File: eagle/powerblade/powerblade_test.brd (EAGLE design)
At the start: 27.9 x 27.9 mm, 78 parts, among them J1 JTAG_14PIN_IDC-NL, J21 AC_INFILM, Q1 2N7002, U1 TPS62122, U2 AD524, U3 MSP430FR5738, U4 LTC5800, U5 MAX9910, U6 MAX9910

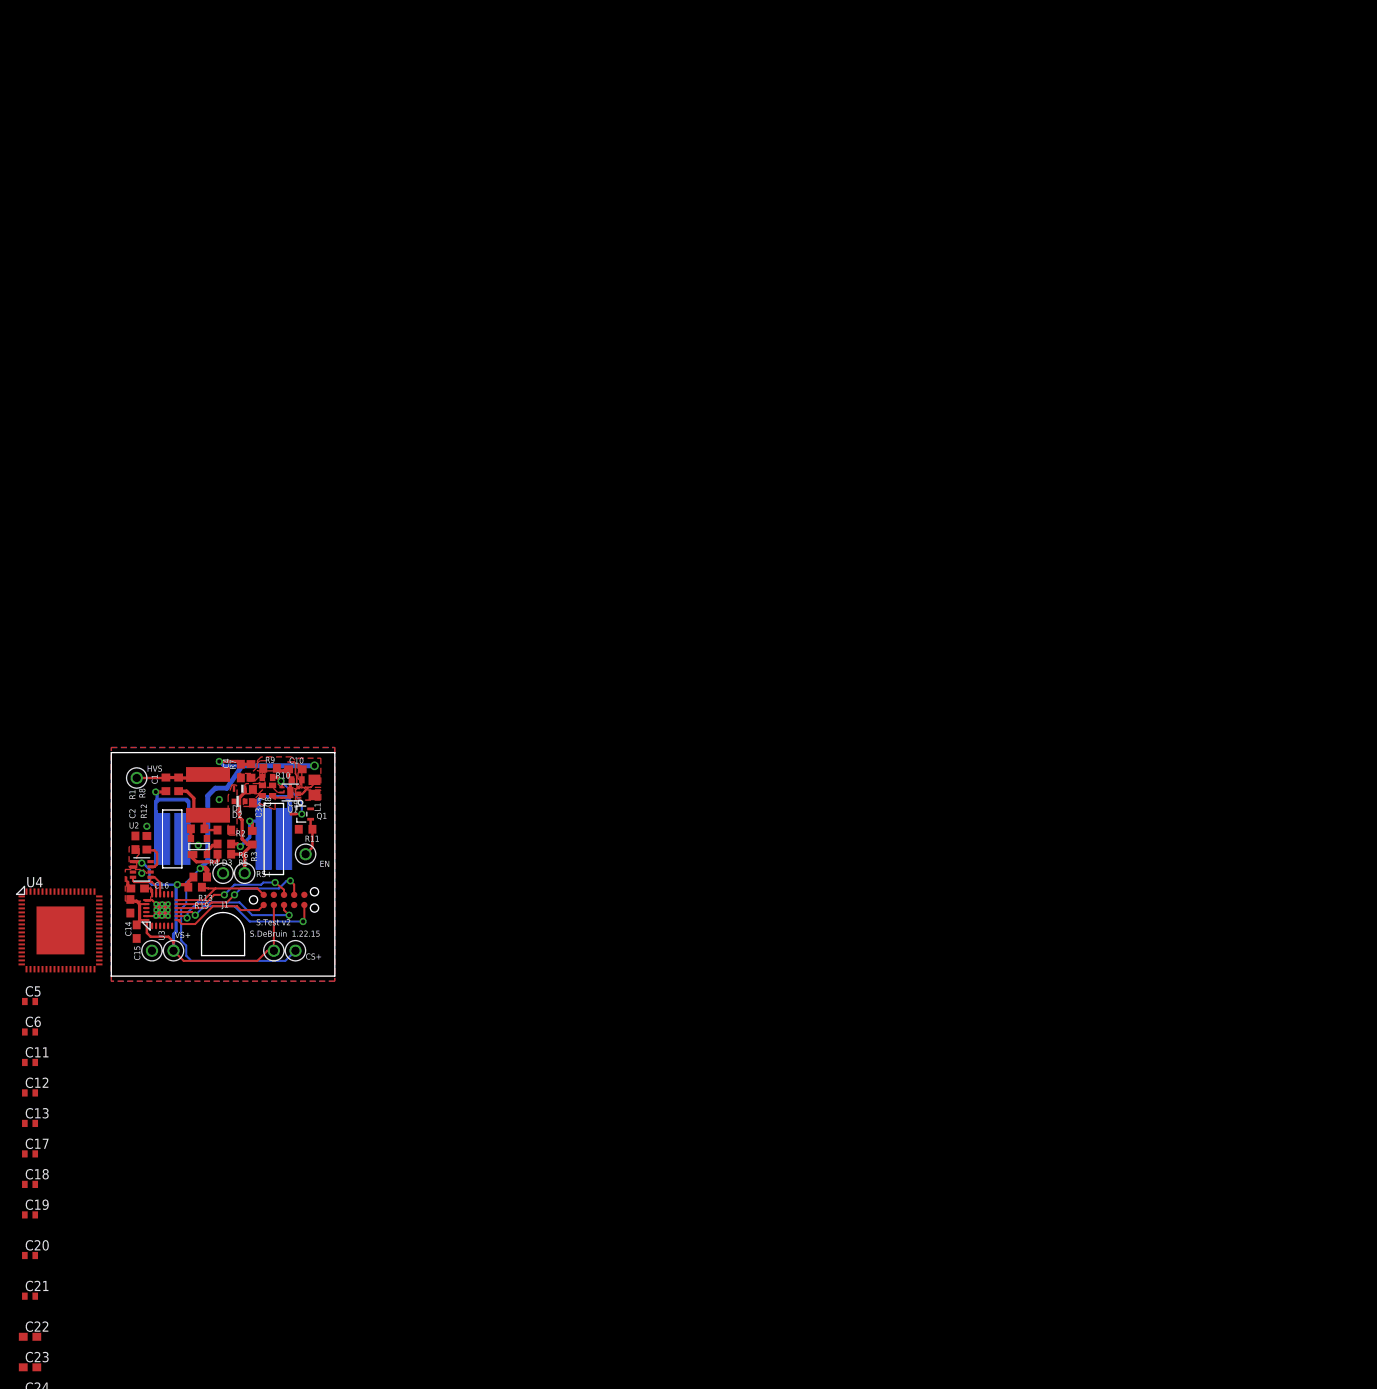
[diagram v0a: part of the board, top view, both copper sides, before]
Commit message: added outline for powerblade test board
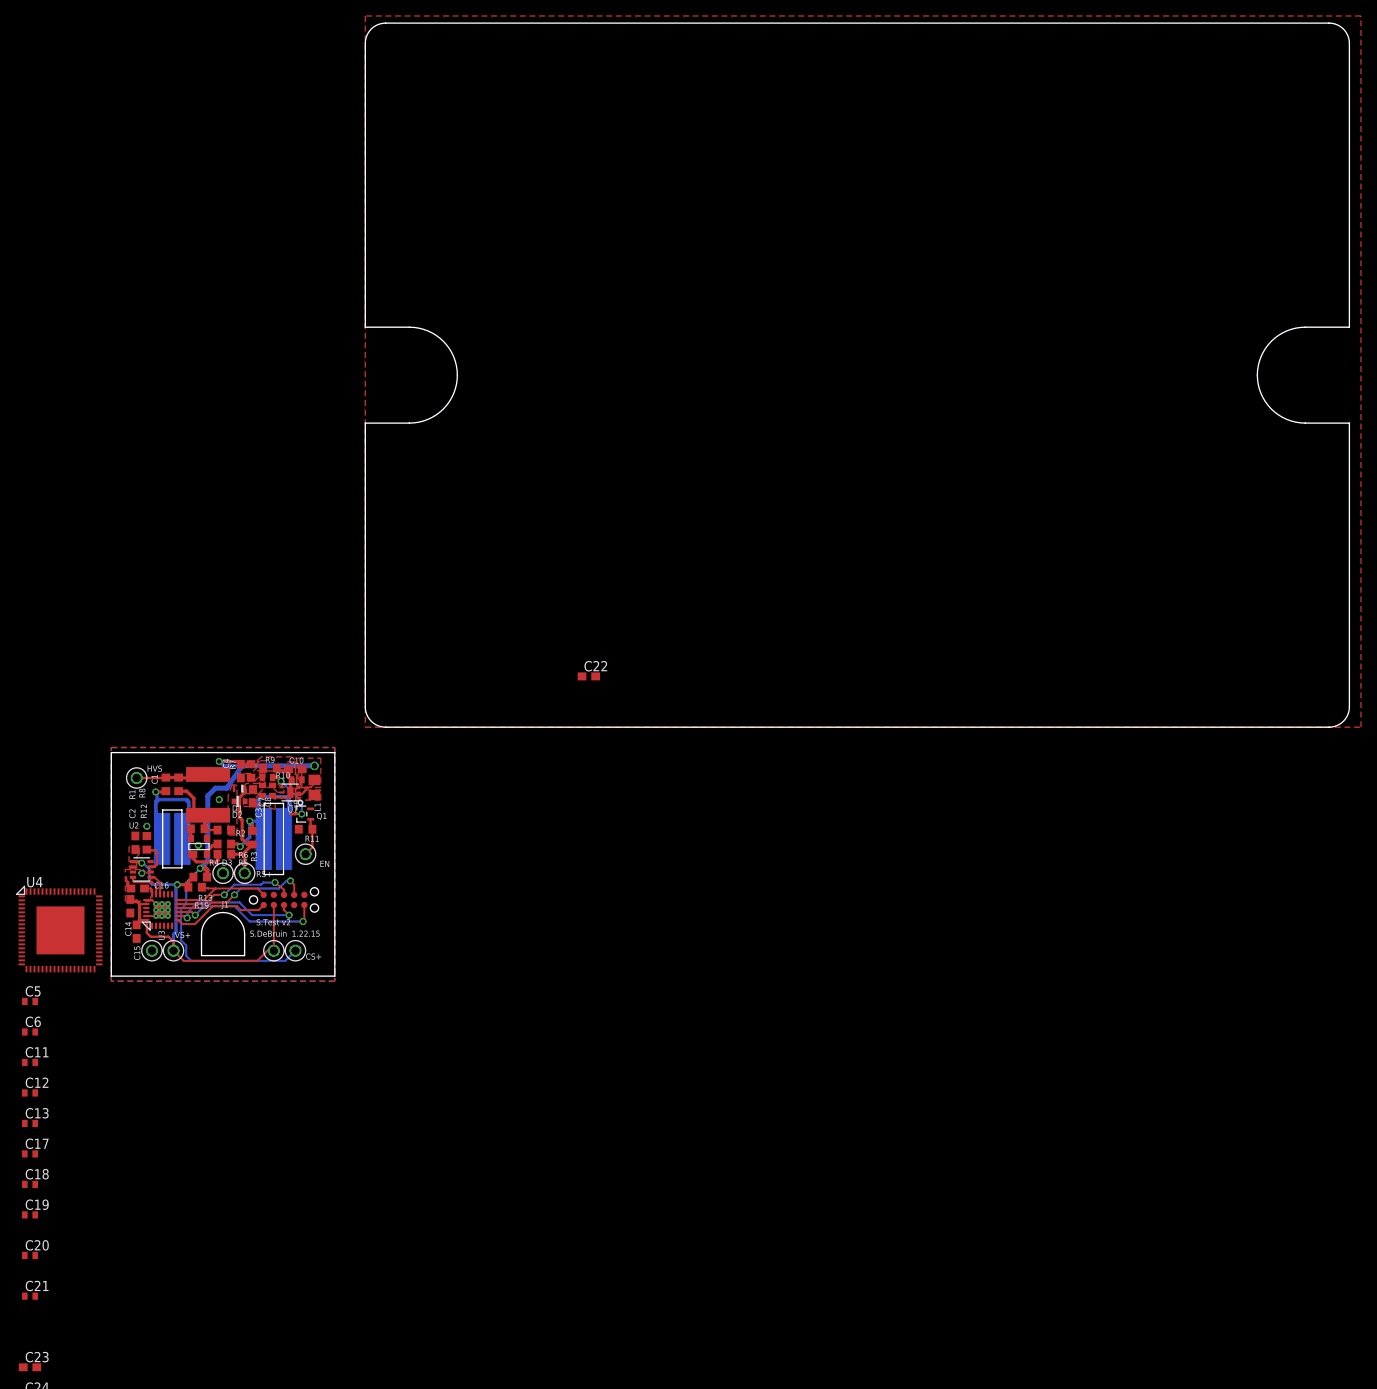
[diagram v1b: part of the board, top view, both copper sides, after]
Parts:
- moved C22 108.1 mm to (27.9, 6.35)
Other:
- board size 27.9 x 27.9 mm -> 123 x 88 mm
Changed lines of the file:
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@@
 <?xml version="1.0" encoding="utf-8"?>
 <!DOCTYPE eagle SYSTEM "eagle.dtd">
-<eagle version="6.5.0">
+<eagle version="6.3">
 <drawing>
 <settings>
@@
 <setting verticaltext="up"/>
 </settings>
-<grid distance="0.05" unitdist="inch" unit="mm" style="lines" multiple="1" display="no" altdistance="6.25" altunitdist="mil" altunit="mil"/>
+<grid distance="0.05" unitdist="inch" unit="mil" style="lines" multiple="1" display="no" altdistance="6.25" altunitdist="mil" altunit="mil"/>
 <layers>
 <layer number="1" name="Top" color="4" fill="1" visible="yes" active="yes"/>
@@
 <text x="-9.2075" y="-26.19375" size="0.762" layer="21">1.22.15</text>
 <text x="-13.6525" y="-24.765" size="0.762" layer="21">S.Test v2</text>
+<wire x1="2.54" y1="0" x2="0" y2="2.54" width="0" layer="20" curve="-90"/>
+<wire x1="0" y1="85.471" x2="2.54" y2="88.011" width="0" layer="20" curve="-90"/>
+<wire x1="2.54" y1="88.011" x2="120.4722" y2="88.011" width="0" layer="20"/>
+<wire x1="120.4722" y1="88.011" x2="123.0122" y2="85.471" width="0" layer="20" curve="-90"/>
+<wire x1="123.0122" y1="2.54" x2="120.4722" y2="0" width="0" layer="20" curve="-90"/>
+<wire x1="120.4722" y1="0" x2="2.54" y2="0" width="0" layer="20"/>
+<wire x1="0" y1="2.54" x2="0" y2="38.0111" width="0" layer="20"/>
+<wire x1="0" y1="38.0111" x2="5.5118" y2="38.0111" width="0" layer="20"/>
+<wire x1="5.5118" y1="38.0111" x2="11.5062" y2="44.0055" width="0" layer="20" curve="90"/>
+<wire x1="11.5062" y1="44.0055" x2="5.5118" y2="49.9999" width="0" layer="20" curve="90"/>
+<wire x1="5.5118" y1="49.9999" x2="0" y2="49.9999" width="0" layer="20"/>
+<wire x1="0" y1="49.9999" x2="0" y2="85.471" width="0" layer="20"/>
+<wire x1="123.0122" y1="2.54" x2="123.0122" y2="38.0111" width="0" layer="20"/>
+<wire x1="123.0122" y1="38.0111" x2="117.5004" y2="38.0111" width="0" layer="20"/>
+<wire x1="117.5004" y1="38.0111" x2="111.506" y2="44.0055" width="0" layer="20" curve="-90"/>
+<wire x1="111.506" y1="44.0055" x2="117.5004" y2="49.9999" width="0" layer="20" curve="-90"/>
+<wire x1="117.5004" y1="49.9999" x2="123.0122" y2="49.9999" width="0" layer="20"/>
+<wire x1="123.0122" y1="49.9999" x2="123.0122" y2="85.471" width="0" layer="20"/>
 </plain>
 <attributes>
@@
 <element name="C20" library="rcl" package="C0402" value="56nF" x="-41.91" y="-66.04"/>
 <element name="C21" library="rcl" package="C0402" value="56nF" x="-41.91" y="-71.12"/>
-<element name="C22" library="rcl" package="C0603" value="0.1uF" x="-41.91" y="-76.2"/>
+<element name="C22" library="rcl" package="C0603" value="0.1uF" x="27.94" y="6.35"/>
 <element name="C23" library="rcl" package="C0603" value="0.47uF" x="-41.91" y="-80.01"/>
 <element name="C24" library="rcl" package="C0603" value="0.22uF" x="-41.91" y="-83.82"/>
@@
 <contactref element="U5" pad="P2"/>
 <contactref element="SV1" pad="8"/>
+<polygon width="0.2032" layer="1">
+<vertex x="0" y="0"/>
+<vertex x="124.46" y="0"/>
+<vertex x="124.46" y="88.9"/>
+<vertex x="0" y="88.9"/>
+</polygon>
 <wire x1="-33.97" y1="-128.27" x2="-33.56" y2="-134.89" width="0" layer="19" extent="1-1"/>
 <wire x1="-37.78" y1="-128.27" x2="-33.97" y2="-128.27" width="0" layer="19" extent="1-1"/>
@@
 <wire x1="-41.06" y1="-83.82" x2="-41.06" y2="-87.63" width="0" layer="19" extent="1-1"/>
 <wire x1="-41.06" y1="-80.01" x2="-41.06" y2="-83.82" width="0" layer="19" extent="1-1"/>
-<wire x1="-41.06" y1="-76.2" x2="-41.06" y2="-80.01" width="0" layer="19" extent="1-1"/>
-<wire x1="-41.26" y1="-71.12" x2="-41.06" y2="-76.2" width="0" layer="19" extent="1-1"/>
+<wire x1="-41.26" y1="-71.12" x2="-41.06" y2="-80.01" width="0" layer="19" extent="1-1"/>
 <wire x1="-41.26" y1="-66.04" x2="-41.26" y2="-71.12" width="0" layer="19" extent="1-1"/>
 <wire x1="-38.1" y1="-25.4" x2="-41.26" y2="-66.04" width="0" layer="19" extent="1-1"/>
 <wire x1="-29.36875" y1="-23.23375" x2="-38.1" y2="-25.4" width="0" layer="19" extent="1-1"/>
-<wire x1="-27.375" y1="-23.61" x2="-29.36875" y2="-23.23375" width="0" layer="19" extent="1-1"/>
-<wire x1="-26.15" y1="-22.86" x2="-26.15" y2="-23.61" width="0" layer="19" extent="1-1"/>
-<wire x1="-25.4" y1="-22.86" x2="-25.4" y2="-23.61" width="0" layer="19" extent="1-1"/>
-<wire x1="-26.15" y1="-22.11" x2="-26.15" y2="-22.86" width="0" layer="19" extent="1-1"/>
-<wire x1="-24.65" y1="-23.61" x2="-25.4" y2="-23.61" width="0" layer="19" extent="1-1"/>
-<wire x1="-29.298" y1="-20.16125" x2="-27.375" y2="-21.61" width="0" layer="19" extent="1-1"/>
-<wire x1="-29.04" y1="-18.105" x2="-29.845" y2="-18.7325" width="0" layer="19" extent="1-1"/>
-<wire x1="-27.94" y1="-18.25625" x2="-29.04" y2="-18.105" width="0" layer="19" extent="1-1"/>
-<wire x1="-26.84" y1="-18.105" x2="-27.94" y2="-18.25625" width="0" layer="19" extent="1-1"/>
-<wire x1="-28.575" y1="-26.40875" x2="-27.375" y2="-23.61" width="0" layer="19" extent="1-1"/>
-<wire x1="-26.67" y1="-27.94" x2="-28.575" y2="-26.40875" width="0" layer="19" extent="1-1"/>
-<wire x1="-28.73375" y1="-13.59625" x2="-29.04" y2="-18.105" width="0" layer="19" extent="1-1"/>
-<wire x1="-27.305" y1="-13.59625" x2="-28.73375" y2="-13.59625" width="0" layer="19" extent="1-1"/>
-<wire x1="-27.305" y1="-12.3825" x2="-27.305" y2="-13.59625" width="0" layer="19" extent="1-1"/>
-<wire x1="-20.8788" y1="-14.76375" x2="-27.305" y2="-13.59625" width="0" layer="19" extent="1-1"/>
-<wire x1="-19.79625" y1="-13.9225" x2="-20.8788" y2="-14.76375" width="0" layer="19" extent="1-1"/>
-<wire x1="-17.78" y1="-18.25625" x2="-20.8788" y2="-14.76375" width="0" layer="19" extent="1-1"/>
-<wire x1="-18.25625" y1="-9.04875" x2="-19.79625" y2="-13.9225" width="0" layer="19" extent="1-1"/>
-<wire x1="-15.01625" y1="-9.271" x2="-18.25625" y2="-9.04875" width="0" layer="19" extent="1-1"/>
-<wire x1="-14.0462" y1="-9.486" x2="-15.01625" y2="-9.271" width="0" layer="19" extent="1-1"/>
-<wire x1="-12.85875" y1="-8.5748" x2="-14.0462" y2="-9.486" width="0" layer="19" extent="1-1"/>
-<wire x1="-11.58875" y1="-8.5748" x2="-12.85875" y2="-8.5748" width="0" layer="19" extent="1-1"/>
-<wire x1="-11.34975" y1="-8.80975" x2="-11.58875" y2="-8.5748" width="0" layer="19" extent="1-1"/>
-<wire x1="-6.8375" y1="-10.2085" x2="-9.36625" y2="-8.79475" width="0" layer="19" extent="1-1"/>
-<wire x1="-8.31125" y1="-12.7635" x2="-6.8375" y2="-10.2085" width="0" layer="19" extent="1-1"/>
-<wire x1="-11.43" y1="-20.955" x2="-17.78" y2="-18.25625" width="0" layer="19" extent="1-1"/>
+<wire x1="28.79" y1="6.35" x2="-6.8375" y2="-10.2085" width="0" layer="19" extent="1-1"/>
 </signal>
 <signal name="VCC">
@@
 <wire x1="-42.76" y1="-97.79" x2="-31.33" y2="-102.87" width="0" layer="19" extent="1-1"/>
 <wire x1="-22.70125" y1="-29.21" x2="-42.76" y2="-97.79" width="0" layer="19" extent="1-1"/>
-<wire x1="-29.04" y1="-17.455" x2="-29.04" y2="-16.805" width="0" layer="19" extent="1-1"/>
-<wire x1="-28.73375" y1="-15.29625" x2="-29.04" y2="-16.805" width="0" layer="19" extent="1-1"/>
 </signal>
 <signal name="RST">
@@
 <contactref element="U4" pad="P30"/>
 <contactref element="C22" pad="1"/>
-<wire x1="-36.85" y1="-30.25" x2="-42.76" y2="-76.2" width="0" layer="19" extent="1-1"/>
+<wire x1="27.09" y1="6.35" x2="-36.85" y2="-30.25" width="0" layer="19" extent="1-1"/>
 </signal>
 <signal name="NRST">
@@
 <contactref element="R20" pad="1"/>
 <contactref element="U6" pad="P1"/>
-<wire x1="-34.71" y1="-118.11" x2="-42.76" y2="-118.11" width="0" layer="19" extent="1-1"/>
-<wire x1="-33.97" y1="-127.62" x2="-34.71" y2="-118.11" width="0" layer="19" extent="1-1"/>
+<wire x1="-34.71" y1="-118.11" x2="-33.97" y2="-127.62" width="0" layer="19" extent="1-1"/>
+<wire x1="-42.76" y1="-118.11" x2="-34.71" y2="-118.11" width="0" layer="19" extent="1-1"/>
 </signal>
 <signal name="V_SENSE">
@@
 </signal>
 </signals>
-<errors>
-</errors>
 </board>
 </drawing>
